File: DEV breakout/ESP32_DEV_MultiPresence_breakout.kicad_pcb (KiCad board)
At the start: 2 copper layers, 55 x 86.5 mm, 14 parts, among them J1 USB_C_Receptacle_Power, J2 JST_SH_01X04, U1 ESP32_DevKit_V1_DOIT, U2 EKMxxxxxxxxx, U3 SEN0395, U4 SEN0395

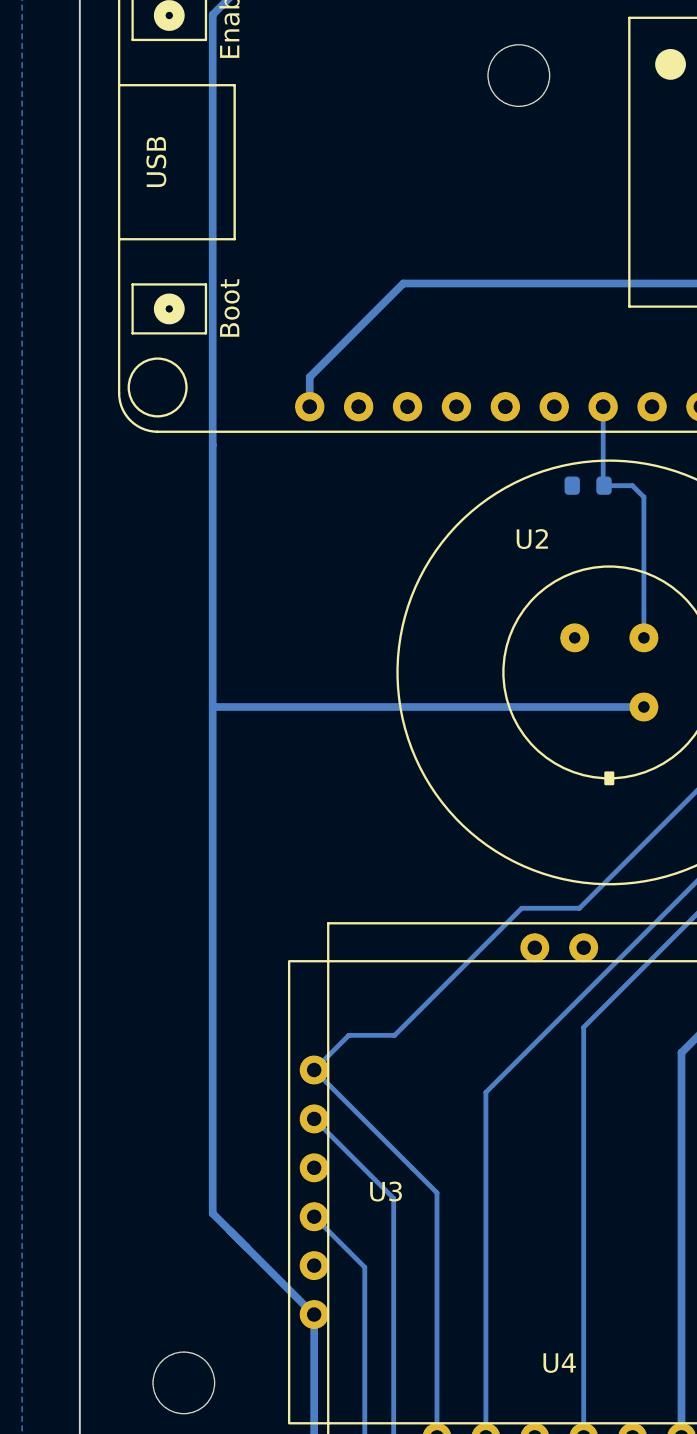
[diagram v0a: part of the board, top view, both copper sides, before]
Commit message: moved 5V line to let more GND thermal connections on the radar
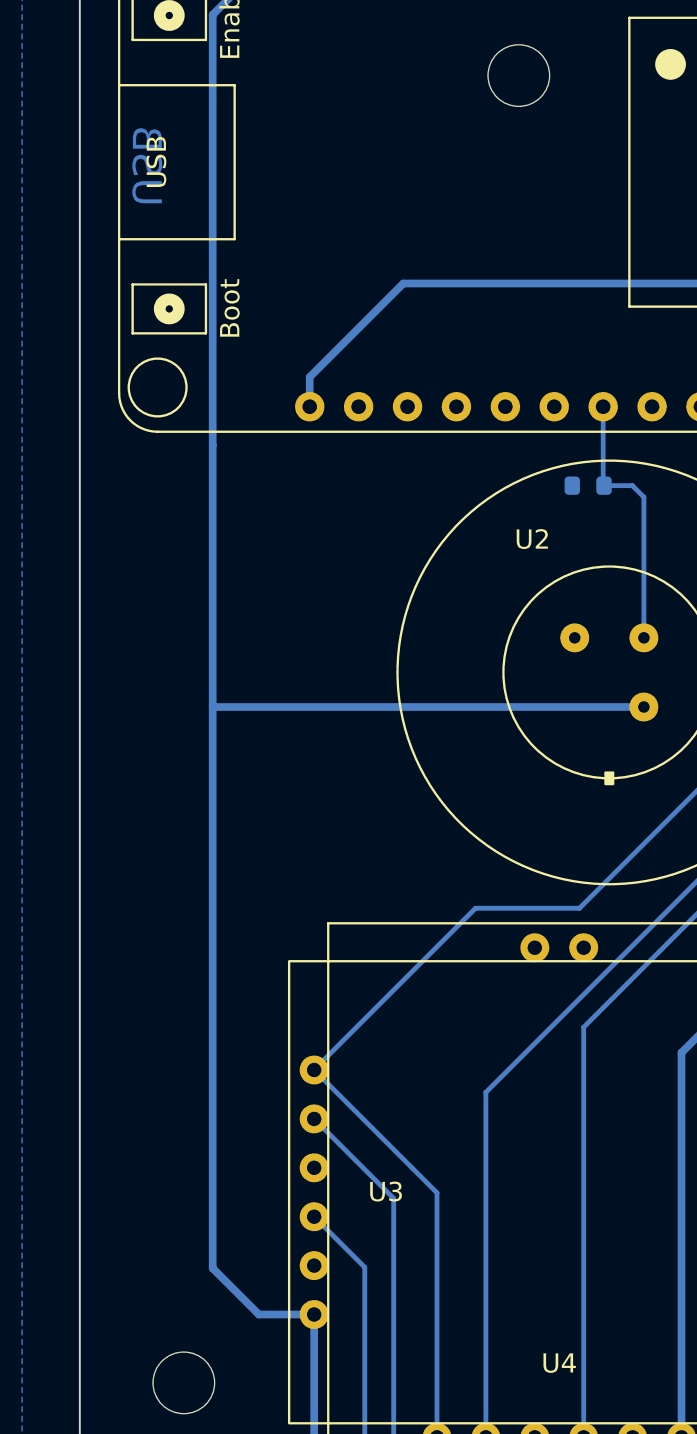
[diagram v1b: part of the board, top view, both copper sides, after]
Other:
- board text added: "USB"
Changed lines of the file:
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@@
   (gr_line (start 115.1 46) (end 115.1 46.1) (layer "Edge.Cuts") (width 0.1))
   (gr_line (start 115.1 132.5) (end 155.7 132.5) (layer "Edge.Cuts") (width 0.1))
+  (gr_text "USB" (at 118.55 61.7 270) (layer "B.Cu")
+    (effects (font (size 1.5 1.5) (thickness 0.3)) (justify mirror))
+  )
   (dimension (type aligned) (layer "User.1")
     (pts (xy 137.8 57) (xy 137.8 46))
@@
   (segment (start 163.3 91.8) (end 163 91.5) (width 0.25) (layer "B.Cu") (net 1))
   (segment (start 163.3 94.895) (end 163.3 91.8) (width 0.25) (layer "B.Cu") (net 1))
-  (segment (start 122.9 117) (end 123.75 117.85) (width 0.4) (layer "B.Cu") (net 2))
   (segment (start 122.096 89.796) (end 122 89.7) (width 0.4) (layer "B.Cu") (net 2))
-  (segment (start 122 116.1) (end 123.75 117.85) (width 0.4) (layer "B.Cu") (net 2))
   (segment (start 160.9 97.9) (end 156.2 97.9) (width 0.4) (layer "B.Cu") (net 2))
   (segment (start 144.396 89.796) (end 122.096 89.796) (width 0.4) (layer "B.Cu") (net 2))
   (segment (start 165.1 96.5) (end 162.6 96.5) (width 0.4) (layer "B.Cu") (net 2))
+  (segment (start 124.4 121.35) (end 122 118.95) (width 0.4) (layer "B.Cu") (net 2))
+  (segment (start 122 118.95) (end 122 89.7) (width 0.4) (layer "B.Cu") (net 2))
   (segment (start 129.7 131) (end 143.08 131) (width 0.4) (layer "B.Cu") (net 2))
-  (segment (start 123.75 117.85) (end 127.25 121.35) (width 0.4) (layer "B.Cu") (net 2))
   (segment (start 162.28 96.18) (end 162.28 94.895) (width 0.4) (layer "B.Cu") (net 2))
   (segment (start 122 53.84) (end 122 76.2) (width 0.4) (layer "B.Cu") (net 2))
   (segment (start 162.6 96.5) (end 162.45 96.35) (width 0.4) (layer "B.Cu") (net 2))
   (segment (start 127.27 121.35) (end 127.27 128.57) (width 0.4) (layer "B.Cu") (net 2))
-  (segment (start 122 89.7) (end 122 116.1) (width 0.4) (layer "B.Cu") (net 2))
   (segment (start 165.32 96.28) (end 165.1 96.5) (width 0.4) (layer "B.Cu") (net 2))
   (segment (start 162.45 96.35) (end 160.9 97.9) (width 0.4) (layer "B.Cu") (net 2))
@@
   (segment (start 127.27 128.57) (end 129.7 131) (width 0.4) (layer "B.Cu") (net 2))
   (segment (start 143.08 131) (end 146.35 127.73) (width 0.4) (layer "B.Cu") (net 2))
+  (segment (start 127.27 121.35) (end 124.4 121.35) (width 0.4) (layer "B.Cu") (net 2))
   (segment (start 127.04 48.8) (end 122 53.84) (width 0.4) (layer "B.Cu") (net 2))
   (segment (start 122 76.2) (end 122 89.7) (width 0.4) (layer "B.Cu") (net 2))
@@
   (segment (start 142.325 78.3) (end 142.28 78.255) (width 0.25) (layer "B.Cu") (net 5))
   (segment (start 133.65 127.73) (end 133.65 115.03) (width 0.25) (layer "B.Cu") (net 6))
-  (segment (start 141.05 100.25) (end 138.05 100.25) (width 0.25) (layer "B.Cu") (net 6))
+  (segment (start 135.65 100.25) (end 127.27 108.63) (width 0.25) (layer "B.Cu") (net 6))
+  (segment (start 148.4 92.9) (end 141.05 100.25) (width 0.25) (layer "B.Cu") (net 6))
+  (segment (start 132.36 113.74) (end 127.27 108.65) (width 0.25) (layer "B.Cu") (net 6))
   (segment (start 148.4 77.55) (end 148.4 92.9) (width 0.25) (layer "B.Cu") (net 6))
-  (segment (start 132.36 113.74) (end 127.27 108.65) (width 0.25) (layer "B.Cu") (net 6))
-  (segment (start 131.45 106.85) (end 129.07 106.85) (width 0.25) (layer "B.Cu") (net 6))
   (segment (start 147.36 76.51) (end 148.4 77.55) (width 0.25) (layer "B.Cu") (net 6))
   (segment (start 147.36 74.2) (end 147.36 76.51) (width 0.25) (layer "B.Cu") (net 6))
-  (segment (start 138.05 100.25) (end 131.45 106.85) (width 0.25) (layer "B.Cu") (net 6))
-  (segment (start 129.07 106.85) (end 127.27 108.65) (width 0.25) (layer "B.Cu") (net 6))
-  (segment (start 148.4 92.9) (end 141.05 100.25) (width 0.25) (layer "B.Cu") (net 6))
+  (segment (start 127.27 108.63) (end 127.27 108.65) (width 0.25) (layer "B.Cu") (net 6))
   (segment (start 133.65 115.03) (end 132.36 113.74) (width 0.25) (layer "B.Cu") (net 6))
+  (segment (start 141.05 100.25) (end 135.65 100.25) (width 0.25) (layer "B.Cu") (net 6))
   (segment (start 134.82 129.1) (end 136.19 127.73) (width 0.25) (layer "B.Cu") (net 7))
   (segment (start 131.4 128.2) (end 132.3 129.1) (width 0.25) (layer "B.Cu") (net 7))

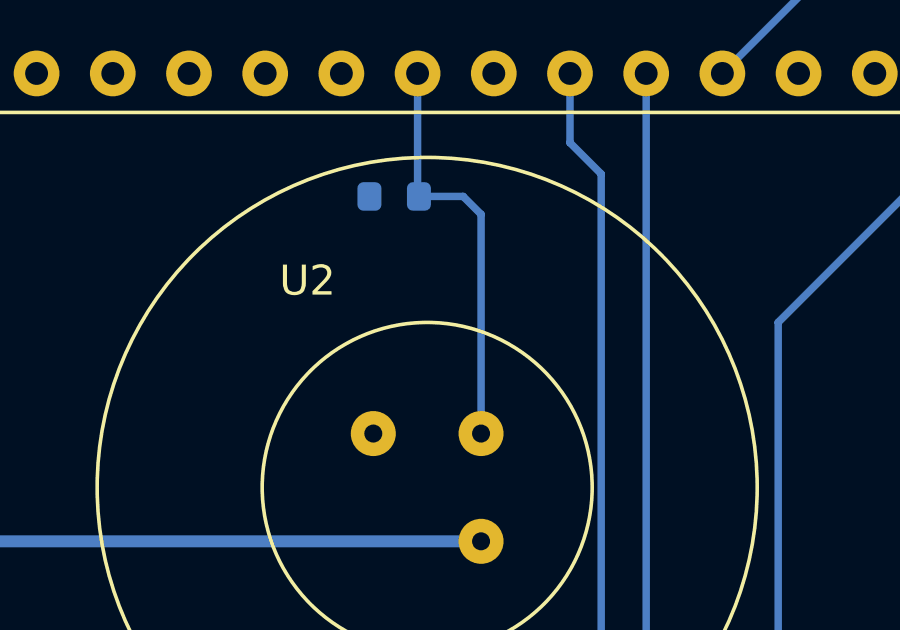
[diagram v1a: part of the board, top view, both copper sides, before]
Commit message: adjusted pir signal trace for nicer routing though the pull down
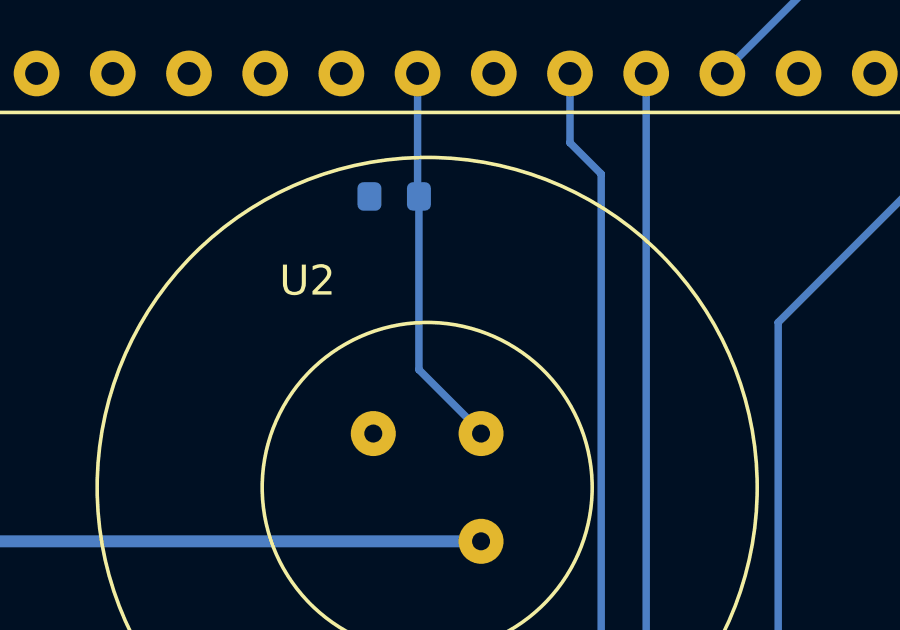
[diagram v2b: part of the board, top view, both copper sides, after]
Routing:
- net motion: track 13.7 -> 12.9 mm
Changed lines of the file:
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@@
   (segment (start 164.6 91.5) (end 164.3 91.8) (width 0.25) (layer "B.Cu") (net 4))
   (segment (start 164.6 90.225) (end 164.6 91.5) (width 0.25) (layer "B.Cu") (net 4))
-  (segment (start 143.8 78.3) (end 142.325 78.3) (width 0.25) (layer "B.Cu") (net 5))
   (segment (start 142.28 78.255) (end 142.28 74.2) (width 0.25) (layer "B.Cu") (net 5))
-  (segment (start 144.396 78.896) (end 143.8 78.3) (width 0.25) (layer "B.Cu") (net 5))
-  (segment (start 144.396 78.896) (end 144.396 86.204) (width 0.25) (layer "B.Cu") (net 5))
+  (segment (start 142.325 84.075) (end 142.325 78.3) (width 0.25) (layer "B.Cu") (net 5))
+  (segment (start 144.396 86.204) (end 144.396 86.146) (width 0.25) (layer "B.Cu") (net 5))
+  (segment (start 144.396 86.146) (end 142.325 84.075) (width 0.25) (layer "B.Cu") (net 5))
   (segment (start 142.325 78.3) (end 142.28 78.255) (width 0.25) (layer "B.Cu") (net 5))
   (segment (start 133.65 127.73) (end 133.65 115.03) (width 0.25) (layer "B.Cu") (net 6))
